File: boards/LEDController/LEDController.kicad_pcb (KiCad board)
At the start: 2 copper layers, 65 x 83 mm, 16 parts, among them J1 ISP, J2 LED1, J3 LED2, J4 Buttons, J5 BoardCon, J6 BoardConOut, J7 LED3, U1 ULN2803A, U2 ATmega48-20P, U4 ULN2803A

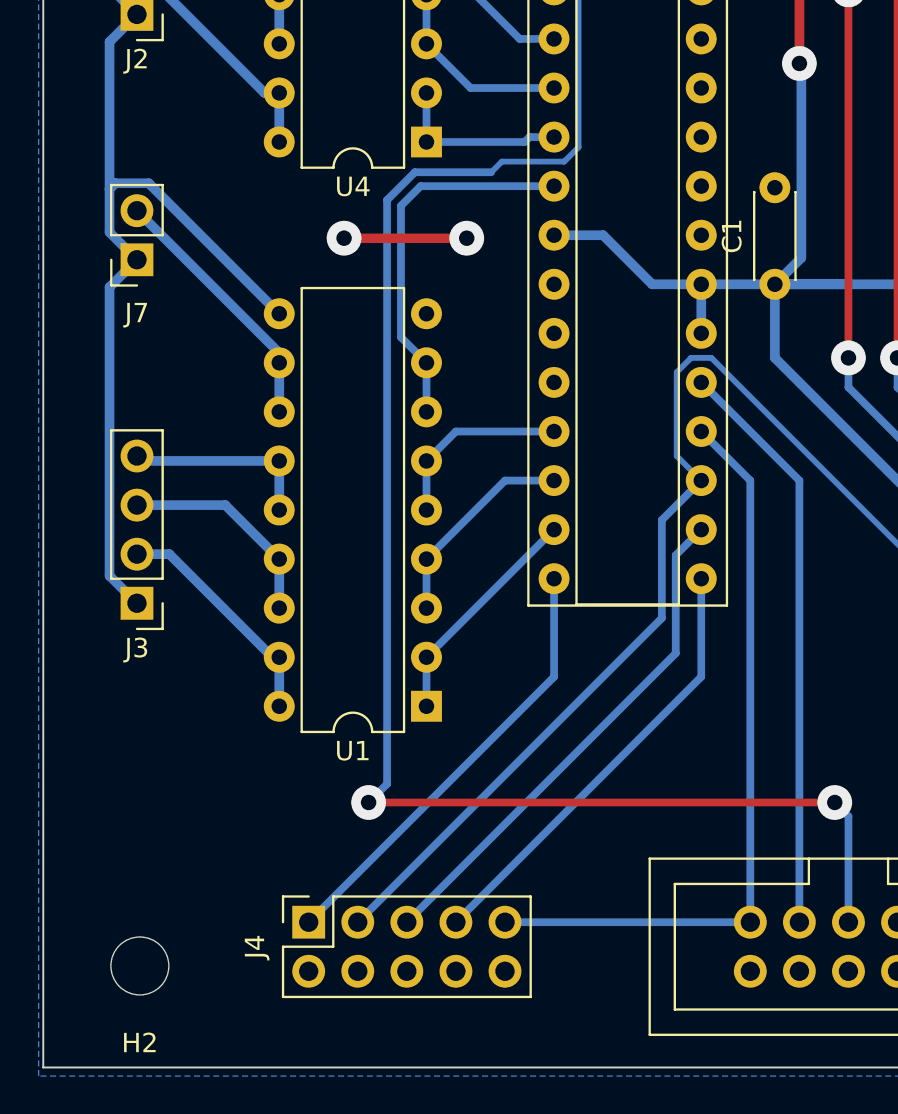
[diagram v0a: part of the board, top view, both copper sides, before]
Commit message: Exported LEDController gerber
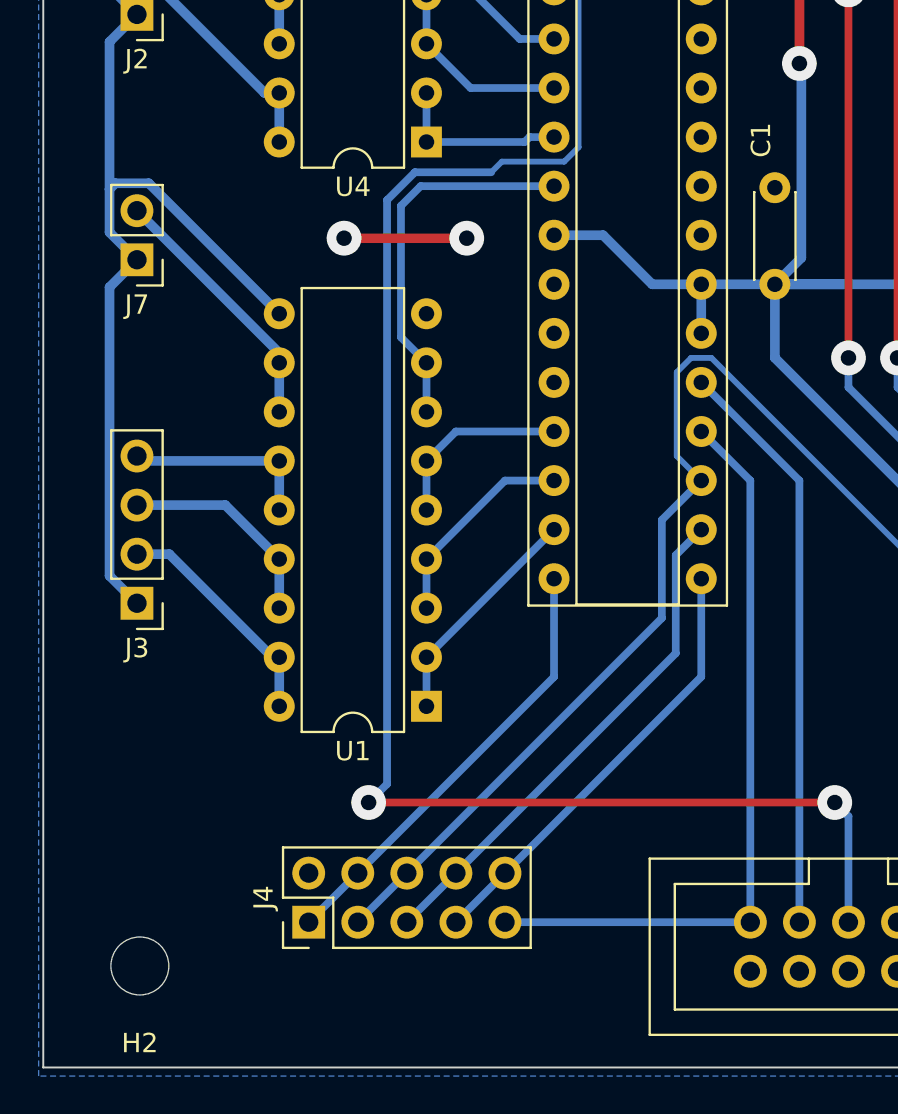
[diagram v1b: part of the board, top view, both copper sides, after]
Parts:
- J4: footprint Connector_PinSocket_2.54mm:PinSocket_2x05_P2.54mm_Vertical -> Connector_PinHeader_2.54mm:PinHeader_2x05_P2.54mm_Vertical
- J7: footprint Connector_PinSocket_2.54mm:PinSocket_1x02_P2.54mm_Vertical -> Connector_PinHeader_2.54mm:PinHeader_1x02_P2.54mm_Vertical
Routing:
- net Net-(J7-Pin_2): track 13.5 -> 13.0 mm

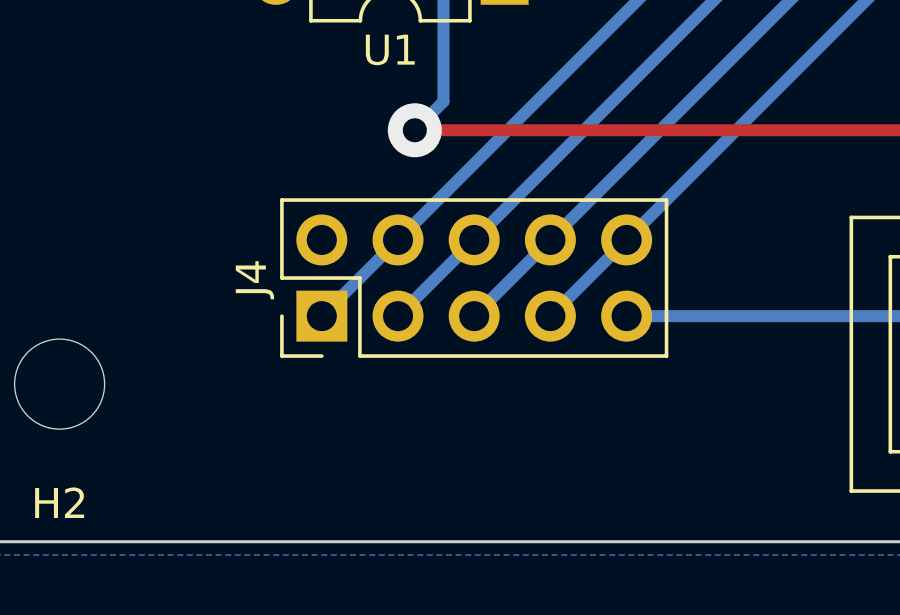
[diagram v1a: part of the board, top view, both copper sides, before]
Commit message: Fixed LEDController button header layout
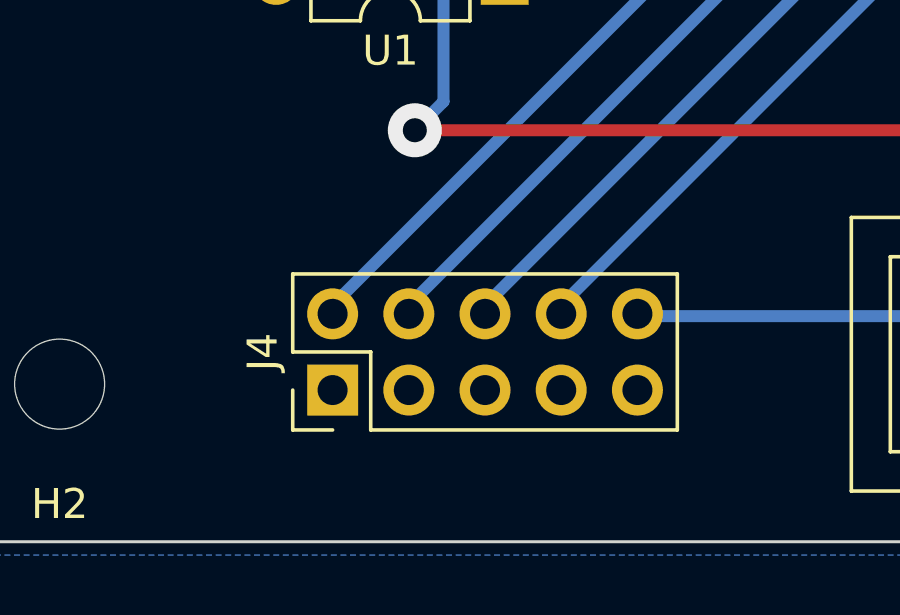
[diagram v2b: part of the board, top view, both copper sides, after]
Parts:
- moved J4 2.49 mm to (129.3, 125.5)
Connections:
- J4 pad 1: Net-(J4-Pin_1) -> GND
- J4 pad 10: GND -> MISO
- J4 pad 2: GND -> Net-(J4-Pin_2)
- J4 pad 3: MOSI -> GND
- J4 pad 4: GND -> MOSI
- J4 pad 5: Net-(J4-Pin_5) -> GND
- J4 pad 6: GND -> Net-(J4-Pin_6)
- J4 pad 7: Net-(J4-Pin_7) -> GND
- J4 pad 8: GND -> Net-(J4-Pin_8)
- J4 pad 9: MISO -> GND
- U2 pad 14: Net-(J4-Pin_1) -> Net-(J4-Pin_2)
- U2 pad 15: Net-(J4-Pin_7) -> Net-(J4-Pin_8)
- U2 pad 16: Net-(J4-Pin_5) -> Net-(J4-Pin_6)
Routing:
- net Net-(J4-Pin_6): track 0.00 -> 26.6 mm
- net Net-(J4-Pin_5): track 26.6 -> 0.00 mm
- net Net-(J4-Pin_8): track 0.00 -> 23.0 mm
- net Net-(J4-Pin_7): track 23.0 -> 0.00 mm
- net Net-(J4-Pin_2): track 0.00 -> 23.0 mm
- net Net-(J4-Pin_1): track 23.0 -> 0.00 mm
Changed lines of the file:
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@@
 	(net 30 "unconnected-(U2-PC1-Pad24)")
 	(net 31 "Net-(U2-PD0)")
-	(net 32 "Net-(J4-Pin_5)")
-	(net 33 "Net-(J4-Pin_1)")
+	(net 32 "Net-(J4-Pin_8)")
+	(net 33 "Net-(J4-Pin_2)")
 	(net 34 "Net-(U2-PD3)")
 	(net 35 "unconnected-(U4-O8-Pad11)")
-	(net 36 "Net-(J4-Pin_7)")
+	(net 36 "Net-(J4-Pin_6)")
 	(net 37 "Net-(J7-Pin_2)")
 	(net 38 "Net-(U1-I7)")
@@
 	(footprint "Connector_PinHeader_2.54mm:PinHeader_2x05_P2.54mm_Vertical"
 		(layer "F.Cu")
-		(at 128.98 123.036052 90)
+		(at 129.34 125.5 90)
 		(descr "Through hole straight pin header, 2x05, 2.54mm pitch, double rows")
 		(tags "Through hole pin header THT 2x05 2.54mm double row")
@@
 			(layers "*.Cu" "*.Mask")
 			(remove_unused_layers no)
-			(net 33 "Net-(J4-Pin_1)")
+			(net 1 "GND")
 			(pinfunction "Pin_1")
 			(pintype "passive")
@@
 			(layers "*.Cu" "*.Mask")
 			(remove_unused_layers no)
-			(net 1 "GND")
+			(net 33 "Net-(J4-Pin_2)")
 			(pinfunction "Pin_2")
 			(pintype "passive")
@@
 			(layers "*.Cu" "*.Mask")
 			(remove_unused_layers no)
-			(net 7 "MOSI")
+			(net 1 "GND")
 			(pinfunction "Pin_3")
 			(pintype "passive")
@@
 			(layers "*.Cu" "*.Mask")
 			(remove_unused_layers no)
-			(net 1 "GND")
+			(net 7 "MOSI")
 			(pinfunction "Pin_4")
 			(pintype "passive")
@@
 			(layers "*.Cu" "*.Mask")
 			(remove_unused_layers no)
-			(net 32 "Net-(J4-Pin_5)")
+			(net 1 "GND")
 			(pinfunction "Pin_5")
 			(pintype "passive")
@@
 			(layers "*.Cu" "*.Mask")
 			(remove_unused_layers no)
-			(net 1 "GND")
+			(net 36 "Net-(J4-Pin_6)")
 			(pinfunction "Pin_6")
 			(pintype "passive")
@@
 			(layers "*.Cu" "*.Mask")
 			(remove_unused_layers no)
-			(net 36 "Net-(J4-Pin_7)")
+			(net 1 "GND")
 			(pinfunction "Pin_7")
 			(pintype "passive")
@@
 			(layers "*.Cu" "*.Mask")
 			(remove_unused_layers no)
-			(net 1 "GND")
+			(net 32 "Net-(J4-Pin_8)")
 			(pinfunction "Pin_8")
 			(pintype "passive")
@@
 			(layers "*.Cu" "*.Mask")
 			(remove_unused_layers no)
-			(net 6 "MISO")
+			(net 1 "GND")
 			(pinfunction "Pin_9")
 			(pintype "passive")
@@
 			(layers "*.Cu" "*.Mask")
 			(remove_unused_layers no)
-			(net 1 "GND")
+			(net 6 "MISO")
 			(pinfunction "Pin_10")
 			(pintype "passive")
@@
 			(layers "*.Cu" "*.Mask")
 			(remove_unused_layers no)
-			(net 33 "Net-(J4-Pin_1)")
+			(net 33 "Net-(J4-Pin_2)")
 			(pinfunction "PB0")
 			(pintype "bidirectional")
@@
 			(layers "*.Cu" "*.Mask")
 			(remove_unused_layers no)
-			(net 36 "Net-(J4-Pin_7)")
+			(net 32 "Net-(J4-Pin_8)")
 			(pinfunction "PB1")
 			(pintype "bidirectional")
@@
 			(layers "*.Cu" "*.Mask")
 			(remove_unused_layers no)
-			(net 32 "Net-(J4-Pin_5)")
+			(net 36 "Net-(J4-Pin_6)")
 			(pinfunction "PB2")
 			(pintype "bidirectional")
@@
 	)
 	(segment
-		(start 147.98 109.116052)
-		(end 147.98 104.036052)
-		(width 0.4)
-		(layer "B.Cu")
-		(net 32)
-	)
-	(segment
-		(start 147.98 104.036052)
-		(end 149.3 102.716052)
+		(start 149.3 110.336052)
+		(end 136.6 123.036052)
 		(width 0.4)
 		(layer "B.Cu")
@@
 	)
 	(segment
-		(start 134.06 123.036052)
-		(end 147.98 109.116052)
+		(start 149.3 105.256052)
+		(end 149.3 110.336052)
 		(width 0.4)
 		(layer "B.Cu")
@@
 	)
 	(segment
-		(start 149.3 110.336052)
-		(end 136.6 123.036052)
+		(start 147.98 109.116052)
+		(end 147.98 104.036052)
 		(width 0.4)
 		(layer "B.Cu")
@@
 	)
 	(segment
-		(start 149.3 105.256052)
-		(end 149.3 110.336052)
+		(start 147.98 104.036052)
+		(end 149.3 102.716052)
+		(width 0.4)
+		(layer "B.Cu")
+		(net 36)
+	)
+	(segment
+		(start 134.06 123.036052)
+		(end 147.98 109.116052)
 		(width 0.4)
 		(layer "B.Cu")
